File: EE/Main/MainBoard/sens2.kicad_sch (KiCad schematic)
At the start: 3 parts, among them J3 Conn_02x13_Odd_Even

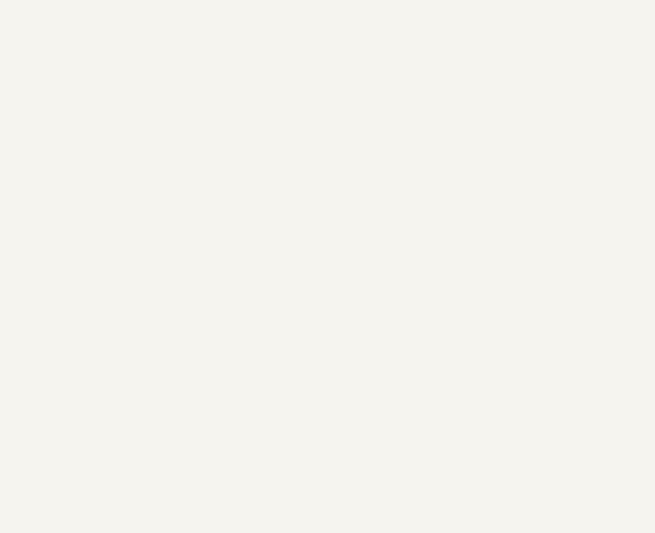
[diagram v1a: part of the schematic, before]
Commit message: WIP - Moving Sensor to IO Expander
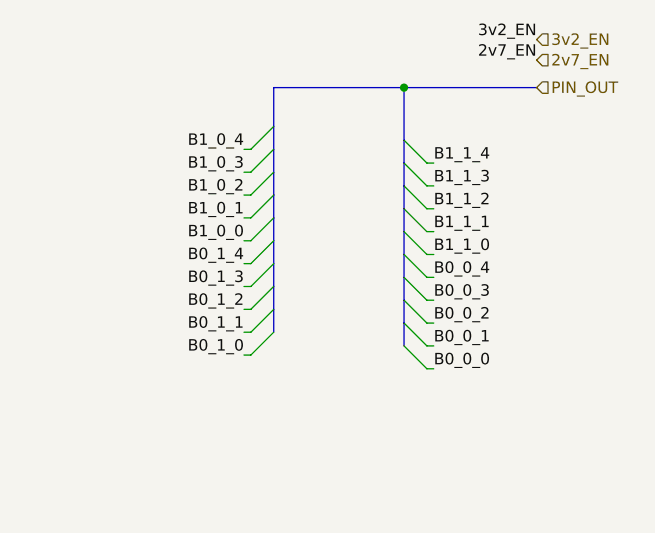
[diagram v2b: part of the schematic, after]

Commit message: Updated layout, and placement for main board
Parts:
- removed J3: Conn_02x13_Odd_Even, Connector_PinHeader_1.27mm:PinHeader_2x13_P1.27mm_Vertical_SMD, symbol Connector_Generic:Conn_02x13_Odd_Even
- added J3: Conn_01x04_Male, Connector_PinSocket_2.54mm:PinSocket_1x04_P2.54mm_Vertical, symbol Connector:Conn_01x04_Male
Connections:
- net GND: now also J3.4 (Pin_4)
- net VCC: now also J3.1 (Pin_1)
- new net SCL: J3.2 (Pin_2)
- new net SDA: J3.3 (Pin_3)
- no-connect marks 2 -> 0

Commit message: Routine Update
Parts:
- H5, H6: footprint MountingHole:MountingHole_2.5mm -> MountingHole:MountingHole_2.7mm
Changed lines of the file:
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@@
       (effects (font (size 1.27 1.27)) (justify left))
     )
-    (property "Footprint" "MountingHole:MountingHole_2.5mm" (id 2) (at 120.65 75.692 0)
+    (property "Footprint" "MountingHole:MountingHole_2.7mm" (id 2) (at 120.65 75.692 0)
       (effects (font (size 1.27 1.27)) hide)
     )
@@
       (effects (font (size 1.27 1.27)) (justify left))
     )
-    (property "Footprint" "MountingHole:MountingHole_2.5mm" (id 2) (at 120.65 119.888 0)
+    (property "Footprint" "MountingHole:MountingHole_2.7mm" (id 2) (at 120.65 119.888 0)
       (effects (font (size 1.27 1.27)) hide)
     )
